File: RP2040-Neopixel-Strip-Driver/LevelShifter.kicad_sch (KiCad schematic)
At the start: 1 part

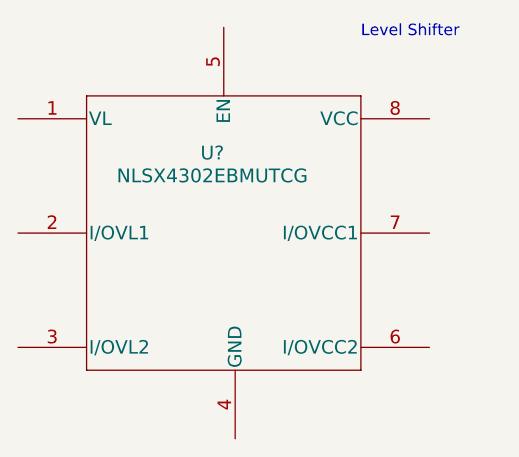
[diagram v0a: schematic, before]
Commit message: Updated all IC symbols to have filled background, personal preference.
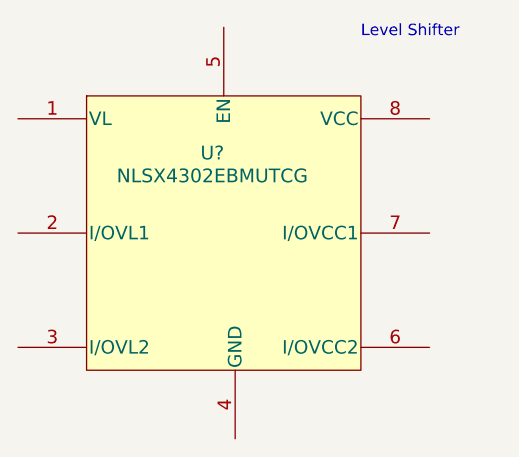
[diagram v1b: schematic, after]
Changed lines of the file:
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@@
       (effects (font (size 1.524 1.524)))
     )
-    (property "Footprint" "NLSX4302EBMUTCG:NLSX4302EBMUTCG" (id 2) (at 102.87 65.024 0)
+    (property "Footprint" "NLSX4302EBMUTCG:NLSX4302EBMUTCG" (id 2) (at 102.87 64.77 0)
       (effects (font (size 1.524 1.524)) hide)
     )

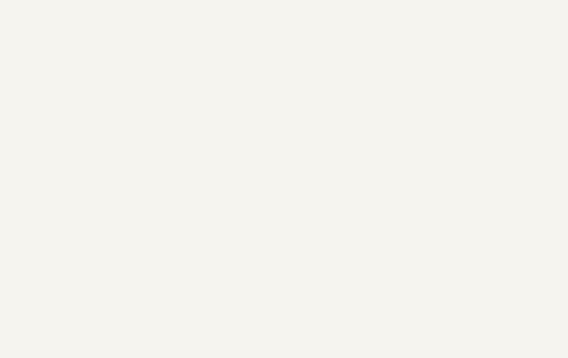
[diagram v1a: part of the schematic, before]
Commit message: Removed RP2040 Schematic, Going with Pico W Module
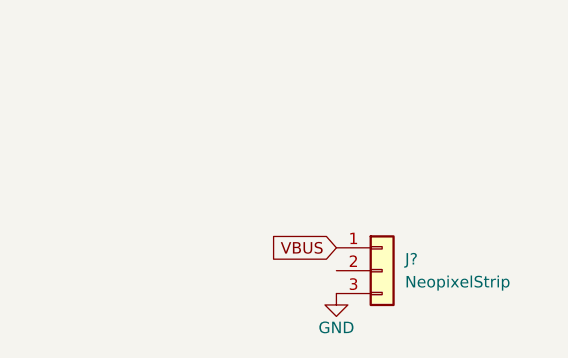
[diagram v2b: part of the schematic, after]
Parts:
- added J?: NeopixelStrip, Breadstick Footprints:NeopixelStrip, symbol Connector_Generic:Conn_01x03
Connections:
- new net GND: J?.3 (Pin_3)
- new net VBUS: J?.1 (Pin_1)
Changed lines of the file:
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@@
     (effects (font (size 1.27 1.27)) (justify left bottom))
+  )
+  (global_label "VBUS" (shape input) (at 134.62 138.43 180) (fields_autoplaced)
+    (effects (font (size 1.27 1.27)) (justify right))
+    (property "Intersheet References" "${INTERSHEET_REFS}" (id 0) (at 127.3083 138.5094 0)
+      (effects (font (size 1.27 1.27)) (justify right) hide)
+    )
+  )
+  (symbol (lib_id "power:GND") (at 134.62 143.51 0) (unit 1)
+    (in_bom yes) (on_board yes)
+    (property "Reference" "#PWR?" (id 0) (at 134.62 149.86 0)
+      (effects (font (size 1.27 1.27)) hide)
+    )
+    (property "Value" "GND" (id 1) (at 134.62 147.32 0))
+    (property "Footprint" "" (id 2) (at 134.62 143.51 0)
+      (effects (font (size 1.27 1.27)) hide)
+    )
+    (property "Datasheet" "" (id 3) (at 134.62 143.51 0)
+      (effects (font (size 1.27 1.27)) hide)
+    )
+    (pin "1")
+  )
+  (symbol (lib_id "Connector_Generic:Conn_01x03") (at 139.7 140.97 0) (unit 1)
+    (in_bom yes) (on_board yes) (fields_autoplaced)
+    (property "Reference" "J?" (id 0) (at 142.24 139.6999 0)
+      (effects (font (size 1.27 1.27)) (justify left))
+    )
+    (property "Value" "NeopixelStrip" (id 1) (at 142.24 142.2399 0)
+      (effects (font (size 1.27 1.27)) (justify left))
+    )
+    (property "Footprint" "Breadstick Footprints:NeopixelStrip" (id 2) (at 139.7 140.97 0)
+      (effects (font (size 1.27 1.27)) hide)
+    )
+    (property "Datasheet" "~" (id 3) (at 139.7 140.97 0)
+      (effects (font (size 1.27 1.27)) hide)
+    )
+    (pin "1")
+    (pin "2")
+    (pin "3")
   )
   (symbol (lib_id "NLSX4302EBMUTCG:NLSX4302EBMUTCG") (at 80.01 73.66 0) (unit 1)
